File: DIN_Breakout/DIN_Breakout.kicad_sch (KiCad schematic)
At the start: 2 parts, among them J1 Matra Alice, J2 Conn_01x08

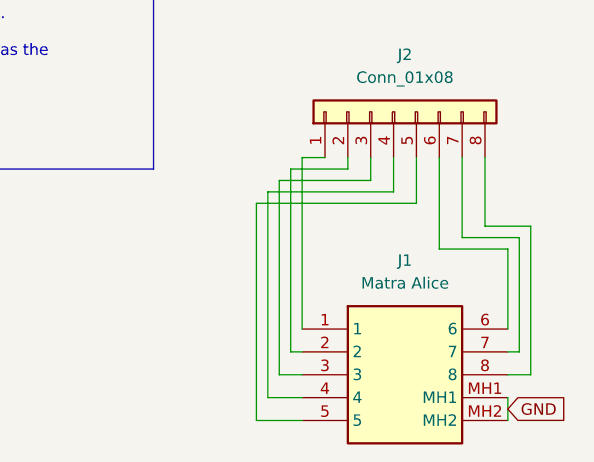
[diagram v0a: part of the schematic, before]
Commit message: Minor typo correction on schematic
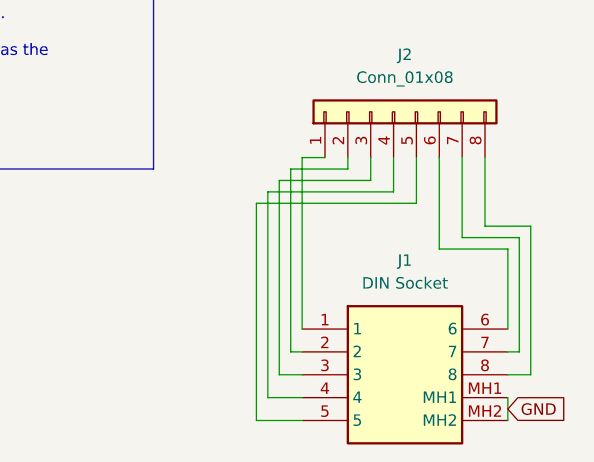
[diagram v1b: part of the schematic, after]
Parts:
- J1: value Matra Alice -> DIN Socket
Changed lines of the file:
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@@
 			)
 		)
-		(property "Value" "Matra Alice"
+		(property "Value" "DIN Socket"
 			(at 111.76 53.34 0)
 			(effects

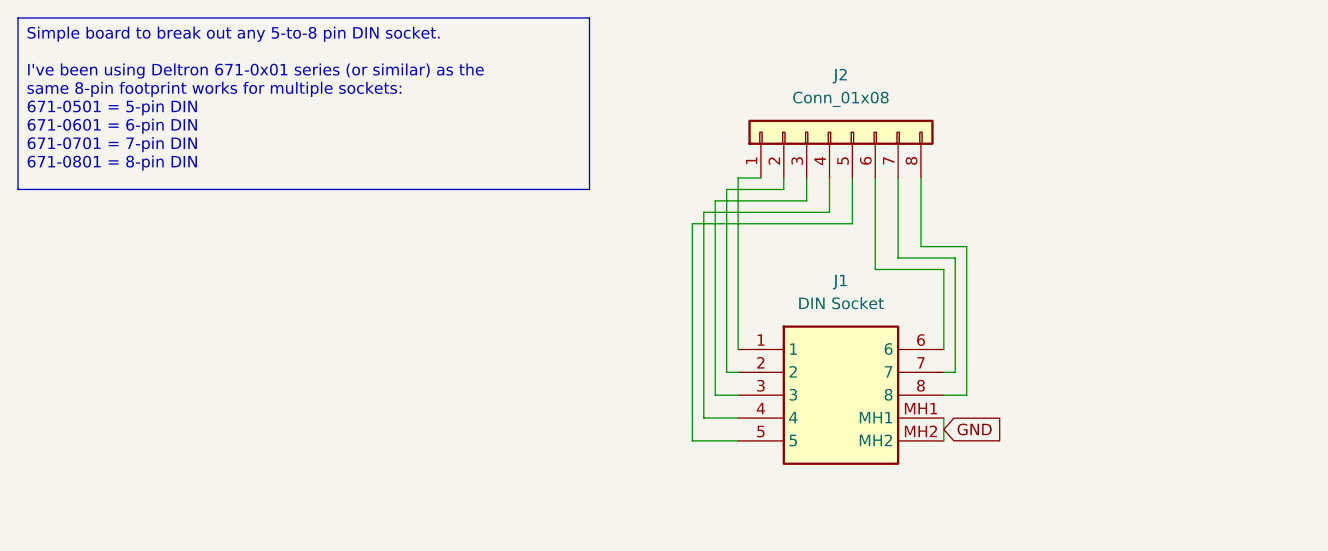
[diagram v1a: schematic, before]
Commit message: Added breakout pin for shield
Sometimes ground is only on shield
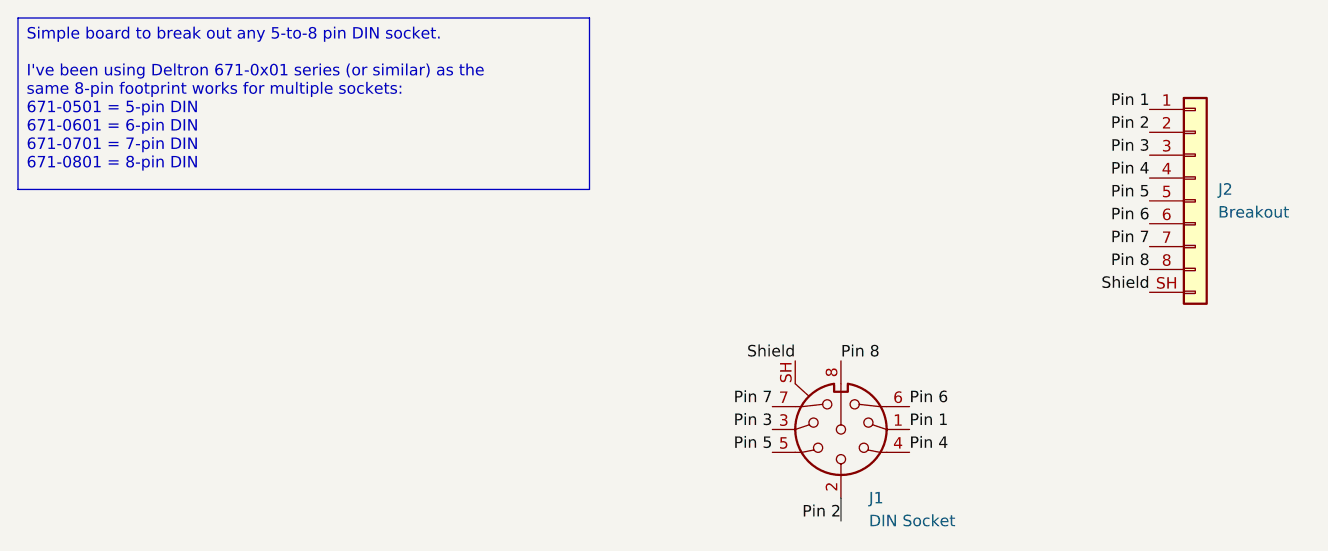
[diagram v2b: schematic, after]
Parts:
- removed J1: DIN Socket, Clueless_Engineer:6710801, symbol Clueless_Engineer:671-0801
- removed J2: Conn_01x08, Connector_PinHeader_2.54mm:PinHeader_1x08_P2.54mm_Vertical, symbol Connector_Generic:Conn_01x08
- added J1: DIN Socket, Clueless_Engineer:SDF80J, symbol Clueless_Engineer:DIN-8
- added J2: Breakout, Connector_PinHeader_2.54mm:PinHeader_1x09_P2.54mm_Vertical, symbol Connector_Generic:Conn_01x09
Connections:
- new net Pin 1: J1.1, J2.1 (Pin_1)
- new net Pin 2: J1.2, J2.2 (Pin_2)
- new net Pin 3: J1.3, J2.3 (Pin_3)
- new net Pin 4: J1.4, J2.4 (Pin_4)
- new net Pin 5: J1.5, J2.5 (Pin_5)
- new net Pin 6: J1.6, J2.6 (Pin_6)
- new net Pin 7: J1.7, J2.7 (Pin_7)
- new net Pin 8: J1.8, J2.8 (Pin_8)
- new net Shield: J1.SH, J2.SH (Pin_9)
